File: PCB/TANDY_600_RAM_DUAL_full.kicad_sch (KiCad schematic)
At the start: 7 parts, among them CN1 TANDY_600_RAM_BUS, CN2 TANDY_600_RAM_BUS, U1 AS6C4008, U2 74HC148, U3 74LVC1G02

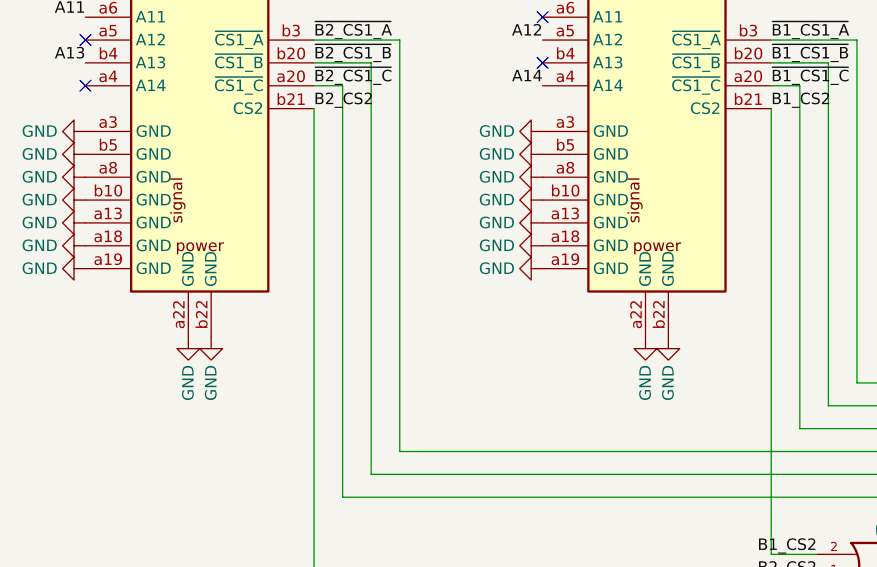
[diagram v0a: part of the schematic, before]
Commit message: add full-size dual
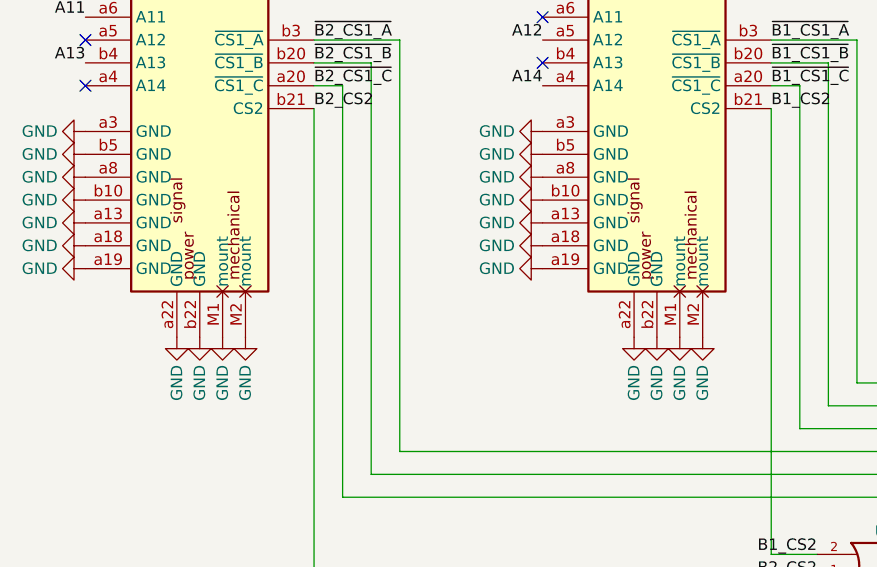
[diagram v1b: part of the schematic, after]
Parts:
- CN1, CN2: footprint 000_LOCAL:DIN41612-2x22_male_vertical_bare_pins -> 000_LOCAL:DIN41612-2x22_male_vertical; symbol 000_LOCAL:TANDY_600_RAM_BUS_plain_pins -> 000_LOCAL:TANDY_600_RAM_BUS
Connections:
- net GND: now also CN1.M1 (mount), CN1.M2 (mount), CN2.M1 (mount), CN2.M2 (mount)
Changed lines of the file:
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@@
     (title "TANDY 600 RAM")
     (date "2022-10-20")
-    (rev "DUAL_005")
+    (rev "DUAL_full_001")
     (company "Brian K. White - b.kenyon.w@gmail.com")
     (comment 1 "LICENSE: CC-BY-SA 4.0")
@@
     (pin "1")
   )
-  (symbol (lib_id "000_LOCAL:TANDY_600_RAM_BUS_plain_pins") (at 107.95 80.01 0) (unit 1)
+  (symbol (lib_id "000_LOCAL:TANDY_600_RAM_BUS") (at 107.95 80.01 0) (unit 1)
     (in_bom yes) (on_board yes) (fields_autoplaced)
     (property "Reference" "CN1" (id 0) (at 113.7794 44.45 0)
@@
       (effects (font (size 1.27 1.27)) (justify left))
     )
-    (property "Footprint" "000_LOCAL:DIN41612-2x22_male_vertical_bare_pins" (id 2) (at 107.95 80.01 0)
+    (property "Footprint" "000_LOCAL:DIN41612-2x22_male_vertical" (id 2) (at 107.95 80.01 0)
       (effects (font (size 1.27 1.27)) hide)
     )
@@
     (pin "b22")
     (pin "b5")
+    (pin "M1")
+    (pin "M2")
     (pin "a10")
     (pin "a11")
@@
     (pin "b9")
   )
-  (symbol (lib_id "000_LOCAL:GND") (at 106.68 115.57 0) (unit 1)
-    (in_bom yes) (on_board yes)
-    (property "Reference" "#PWR0113" (id 0) (at 106.68 121.92 0)
-      (effects (font (size 1.27 1.27)) hide)
-    )
-    (property "Value" "GND" (id 1) (at 106.68 120.65 90))
-    (property "Footprint" "" (id 2) (at 106.68 115.57 0)
-      (effects (font (size 1.27 1.27)) hide)
-    )
-    (property "Datasheet" "" (id 3) (at 106.68 115.57 0)
+  (symbol (lib_id "000_LOCAL:GND") (at 59.69 115.57 0) (unit 1)
+    (in_bom yes) (on_board yes)
+    (property "Reference" "#PWR0111" (id 0) (at 59.69 121.92 0)
+      (effects (font (size 1.27 1.27)) hide)
+    )
+    (property "Value" "GND" (id 1) (at 59.69 120.65 90))
+    (property "Footprint" "" (id 2) (at 59.69 115.57 0)
+      (effects (font (size 1.27 1.27)) hide)
+    )
+    (property "Datasheet" "" (id 3) (at 59.69 115.57 0)
+      (effects (font (size 1.27 1.27)) hide)
+    )
+    (pin "1")
+  )
+  (symbol (lib_id "000_LOCAL:GND") (at 105.41 115.57 0) (unit 1)
+    (in_bom yes) (on_board yes)
+    (property "Reference" "#PWR0113" (id 0) (at 105.41 121.92 0)
+      (effects (font (size 1.27 1.27)) hide)
+    )
+    (property "Value" "GND" (id 1) (at 105.41 120.65 90))
+    (property "Footprint" "" (id 2) (at 105.41 115.57 0)
+      (effects (font (size 1.27 1.27)) hide)
+    )
+    (property "Datasheet" "" (id 3) (at 105.41 115.57 0)
       (effects (font (size 1.27 1.27)) hide)
     )
@@
     (pin "1")
   )
-  (symbol (lib_id "000_LOCAL:GND") (at 109.22 115.57 0) (unit 1)
-    (in_bom yes) (on_board yes)
-    (property "Reference" "#PWR0114" (id 0) (at 109.22 121.92 0)
-      (effects (font (size 1.27 1.27)) hide)
-    )
-    (property "Value" "GND" (id 1) (at 109.22 120.65 90))
-    (property "Footprint" "" (id 2) (at 109.22 115.57 0)
-      (effects (font (size 1.27 1.27)) hide)
-    )
-    (property "Datasheet" "" (id 3) (at 109.22 115.57 0)
+  (symbol (lib_id "000_LOCAL:GND") (at 62.23 115.57 0) (unit 1)
+    (in_bom yes) (on_board yes)
+    (property "Reference" "#PWR0112" (id 0) (at 62.23 121.92 0)
+      (effects (font (size 1.27 1.27)) hide)
+    )
+    (property "Value" "GND" (id 1) (at 62.23 120.65 90))
+    (property "Footprint" "" (id 2) (at 62.23 115.57 0)
+      (effects (font (size 1.27 1.27)) hide)
+    )
+    (property "Datasheet" "" (id 3) (at 62.23 115.57 0)
+      (effects (font (size 1.27 1.27)) hide)
+    )
+    (pin "1")
+  )
+  (symbol (lib_id "000_LOCAL:GND") (at 107.95 115.57 0) (unit 1)
+    (in_bom yes) (on_board yes)
+    (property "Reference" "#PWR0114" (id 0) (at 107.95 121.92 0)
+      (effects (font (size 1.27 1.27)) hide)
+    )
+    (property "Value" "GND" (id 1) (at 107.95 120.65 90))
+    (property "Footprint" "" (id 2) (at 107.95 115.57 0)
+      (effects (font (size 1.27 1.27)) hide)
+    )
+    (property "Datasheet" "" (id 3) (at 107.95 115.57 0)
       (effects (font (size 1.27 1.27)) hide)
     )
@@
     (pin "1")
     (pin "2")
+  )
+  (symbol (lib_id "000_LOCAL:GND") (at 113.03 115.57 0) (unit 1)
+    (in_bom yes) (on_board yes)
+    (property "Reference" "#PWR0118" (id 0) (at 113.03 121.92 0)
+      (effects (font (size 1.27 1.27)) hide)
+    )
+    (property "Value" "GND" (id 1) (at 113.03 120.65 90))
+    (property "Footprint" "" (id 2) (at 113.03 115.57 0)
+      (effects (font (size 1.27 1.27)) hide)
+    )
+    (property "Datasheet" "" (id 3) (at 113.03 115.57 0)
+      (effects (font (size 1.27 1.27)) hide)
+    )
+    (pin "1")
   )
   (symbol (lib_id "000_LOCAL:GND") (at 95.25 102.87 270) (unit 1)
@@
     (pin "9")
   )
-  (symbol (lib_id "000_LOCAL:GND") (at 55.88 115.57 0) (unit 1)
-    (in_bom yes) (on_board yes)
-    (property "Reference" "#PWR0119" (id 0) (at 55.88 121.92 0)
-      (effects (font (size 1.27 1.27)) hide)
-    )
-    (property "Value" "GND" (id 1) (at 55.88 120.65 90))
-    (property "Footprint" "" (id 2) (at 55.88 115.57 0)
-      (effects (font (size 1.27 1.27)) hide)
-    )
-    (property "Datasheet" "" (id 3) (at 55.88 115.57 0)
+  (symbol (lib_id "000_LOCAL:GND") (at 54.61 115.57 0) (unit 1)
+    (in_bom yes) (on_board yes)
+    (property "Reference" "#PWR0119" (id 0) (at 54.61 121.92 0)
+      (effects (font (size 1.27 1.27)) hide)
+    )
+    (property "Value" "GND" (id 1) (at 54.61 120.65 90))
+    (property "Footprint" "" (id 2) (at 54.61 115.57 0)
+      (effects (font (size 1.27 1.27)) hide)
+    )
+    (property "Datasheet" "" (id 3) (at 54.61 115.57 0)
       (effects (font (size 1.27 1.27)) hide)
     )
@@
     (pin "1")
   )
+  (symbol (lib_id "000_LOCAL:GND") (at 110.49 115.57 0) (unit 1)
+    (in_bom yes) (on_board yes)
+    (property "Reference" "#PWR0116" (id 0) (at 110.49 121.92 0)
+      (effects (font (size 1.27 1.27)) hide)
+    )
+    (property "Value" "GND" (id 1) (at 110.49 120.65 90))
+    (property "Footprint" "" (id 2) (at 110.49 115.57 0)
+      (effects (font (size 1.27 1.27)) hide)
+    )
+    (property "Datasheet" "" (id 3) (at 110.49 115.57 0)
+      (effects (font (size 1.27 1.27)) hide)
+    )
+    (pin "1")
+  )
   (symbol (lib_id "000_LOCAL:GND") (at 95.25 105.41 270) (unit 1)
     (in_bom yes) (on_board yes)
@@
     (pin "1")
   )
-  (symbol (lib_id "000_LOCAL:GND") (at 58.42 115.57 0) (unit 1)
-    (in_bom yes) (on_board yes)
-    (property "Reference" "#PWR0117" (id 0) (at 58.42 121.92 0)
-      (effects (font (size 1.27 1.27)) hide)
-    )
-    (property "Value" "GND" (id 1) (at 58.42 120.65 90))
-    (property "Footprint" "" (id 2) (at 58.42 115.57 0)
-      (effects (font (size 1.27 1.27)) hide)
-    )
-    (property "Datasheet" "" (id 3) (at 58.42 115.57 0)
+  (symbol (lib_id "000_LOCAL:GND") (at 57.15 115.57 0) (unit 1)
+    (in_bom yes) (on_board yes)
+    (property "Reference" "#PWR0117" (id 0) (at 57.15 121.92 0)
+      (effects (font (size 1.27 1.27)) hide)
+    )
+    (property "Value" "GND" (id 1) (at 57.15 120.65 90))
+    (property "Footprint" "" (id 2) (at 57.15 115.57 0)
+      (effects (font (size 1.27 1.27)) hide)
+    )
+    (property "Datasheet" "" (id 3) (at 57.15 115.57 0)
       (effects (font (size 1.27 1.27)) hide)
     )
@@
     (pin "1")
   )
-  (symbol (lib_name "TANDY_600_RAM_BUS_plain_pins_1") (lib_id "000_LOCAL:TANDY_600_RAM_BUS_plain_pins") (at 57.15 80.01 0) (unit 1)
+  (symbol (lib_id "000_LOCAL:TANDY_600_RAM_BUS") (at 57.15 80.01 0) (unit 1)
     (in_bom yes) (on_board yes) (fields_autoplaced)
     (property "Reference" "CN2" (id 0) (at 62.9794 44.45 0)
@@
       (effects (font (size 1.27 1.27)) (justify left))
     )
-    (property "Footprint" "000_LOCAL:DIN41612-2x22_male_vertical_bare_pins" (id 2) (at 57.15 80.01 0)
+    (property "Footprint" "000_LOCAL:DIN41612-2x22_male_vertical" (id 2) (at 57.15 80.01 0)
       (effects (font (size 1.27 1.27)) hide)
     )
@@
     (pin "b22")
     (pin "b5")
+    (pin "M1")
+    (pin "M2")
     (pin "a10")
     (pin "a11")
@@
       (reference "#PWR0110") (unit 1) (value "GND") (footprint "")
     )
+    (path "/13ba2950-7a48-404e-9344-9a78423336c1"
+      (reference "#PWR0111") (unit 1) (value "GND") (footprint "")
+    )
+    (path "/72476e9e-1a17-42d4-8b96-e5ca0797b835"
+      (reference "#PWR0112") (unit 1) (value "GND") (footprint "")
+    )
     (path "/19fc5179-aee6-44e9-91a4-006db27ac367"
       (reference "#PWR0113") (unit 1) (value "GND") (footprint "")
@@
       (reference "#PWR0115") (unit 1) (value "VMEM") (footprint "")
     )
+    (path "/af84b8d5-0a6a-441c-a4d0-021b7e62304f"
+      (reference "#PWR0116") (unit 1) (value "GND") (footprint "")
+    )
     (path "/ddd0f903-8f6f-4dad-a6bf-1be766e5f808"
       (reference "#PWR0117") (unit 1) (value "GND") (footprint "")
     )
+    (path "/78fdb51c-38fe-4d9b-95ec-f51b5af440c0"
+      (reference "#PWR0118") (unit 1) (value "GND") (footprint "")
+    )
     (path "/9204f334-1c6c-4aa1-959f-4800389620de"
       (reference "#PWR0119") (unit 1) (value "GND") (footprint "")
@@
     )
     (path "/13373e06-954d-4aed-a080-48347e0880c4"
-      (reference "CN1") (unit 1) (value "TANDY_600_RAM_BUS") (footprint "000_LOCAL:DIN41612-2x22_male_vertical_bare_pins")
+      (reference "CN1") (unit 1) (value "TANDY_600_RAM_BUS") (footprint "000_LOCAL:DIN41612-2x22_male_vertical")
     )
     (path "/f210ac00-25e3-4b3d-bd77-536f4a48c2ed"
-      (reference "CN2") (unit 1) (value "TANDY_600_RAM_BUS") (footprint "000_LOCAL:DIN41612-2x22_male_vertical_bare_pins")
+      (reference "CN2") (unit 1) (value "TANDY_600_RAM_BUS") (footprint "000_LOCAL:DIN41612-2x22_male_vertical")
     )
     (path "/00000000-0000-0000-0000-0000613c8a04"

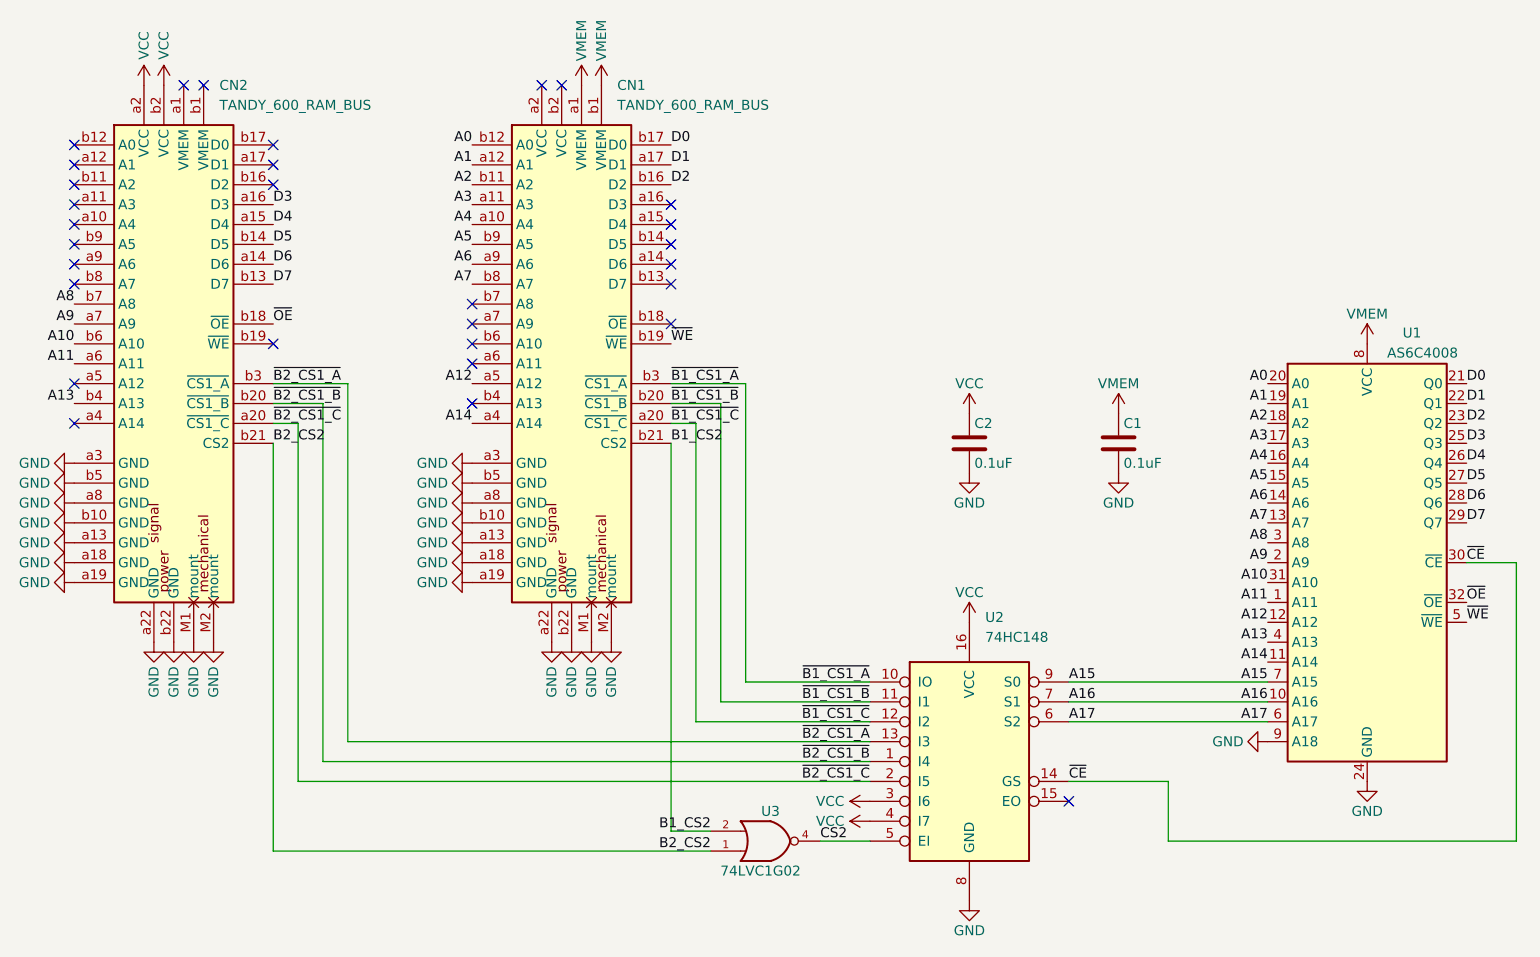
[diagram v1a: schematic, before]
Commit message: footprints, ground paths
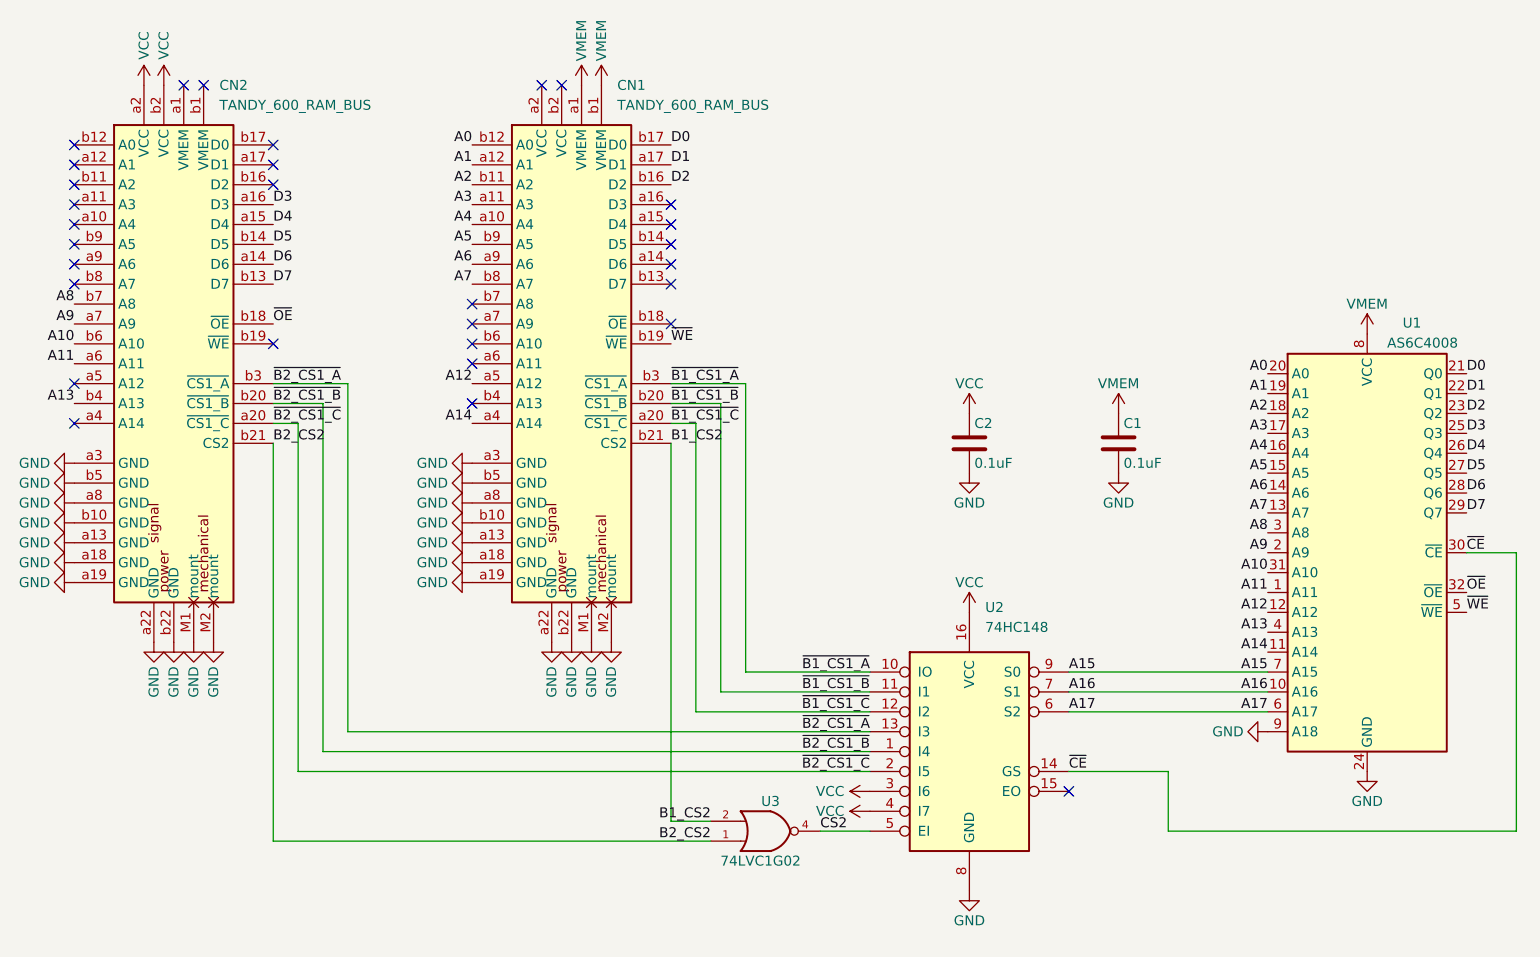
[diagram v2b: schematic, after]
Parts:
- CN1, CN2: footprint 000_LOCAL:DIN41612-2x22_male_vertical -> 000_LOCAL:DIN-41612_02x22_male_vertical
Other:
- moved on the sheet: U1, U2, U3
